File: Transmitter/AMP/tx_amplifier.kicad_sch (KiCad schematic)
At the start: 20 parts, among them J1 Conn_Coaxial, J2 Conn_Coaxial, J3 Screw_Terminal_01x02, Q1 BFR740L3RH

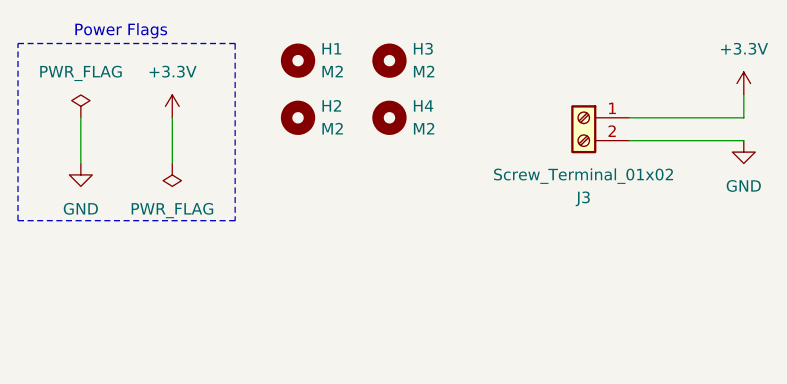
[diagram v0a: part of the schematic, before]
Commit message: tx amplifier v1.1
Change M2 to M3 screws
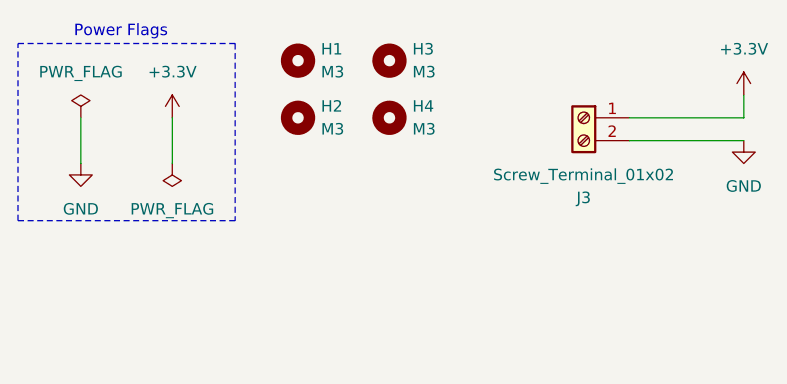
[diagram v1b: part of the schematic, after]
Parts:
- H1, H2, H3, H4: value M2 -> M3; footprint MountingHole:MountingHole_2.2mm_M2_ISO7380 -> MountingHole:MountingHole_3.2mm_M3_ISO7380
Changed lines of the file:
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@@
 	(title_block
 		(title "Amplificador TX")
-		(date "2025-01-07")
-		(rev "v1.0")
+		(date "2025-01-09")
+		(rev "v1.1")
 		(company "Cotti Nicolas Gabriel")
 		(comment 1 "ncotti@frba.utn.edu.ar")
@@
 			)
 		)
-		(property "Value" "M2"
+		(property "Value" "M3"
 			(at 60.96 25.3999 0)
 			(effects
@@
 			)
 		)
-		(property "Footprint" "MountingHole:MountingHole_2.2mm_M2_ISO7380"
+		(property "Footprint" "MountingHole:MountingHole_3.2mm_M3_ISO7380"
 			(at 58.42 24.13 0)
 			(effects
@@
 			)
 		)
-		(property "Value" "M2"
+		(property "Value" "M3"
 			(at 50.8 25.3999 0)
 			(effects
@@
 			)
 		)
-		(property "Footprint" "MountingHole:MountingHole_2.2mm_M2_ISO7380"
+		(property "Footprint" "MountingHole:MountingHole_3.2mm_M3_ISO7380"
 			(at 48.26 24.13 0)
 			(effects
@@
 			)
 		)
-		(property "Value" "M2"
+		(property "Value" "M3"
 			(at 60.96 19.0499 0)
 			(effects
@@
 			)
 		)
-		(property "Footprint" "MountingHole:MountingHole_2.2mm_M2_ISO7380"
+		(property "Footprint" "MountingHole:MountingHole_3.2mm_M3_ISO7380"
 			(at 58.42 17.78 0)
 			(effects
@@
 			)
 		)
-		(property "Value" "M2"
+		(property "Value" "M3"
 			(at 50.8 19.0499 0)
 			(effects
@@
 			)
 		)
-		(property "Footprint" "MountingHole:MountingHole_2.2mm_M2_ISO7380"
+		(property "Footprint" "MountingHole:MountingHole_3.2mm_M3_ISO7380"
 			(at 48.26 17.78 0)
 			(effects
